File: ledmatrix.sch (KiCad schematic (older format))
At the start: 89 parts, among them U58 sled1735

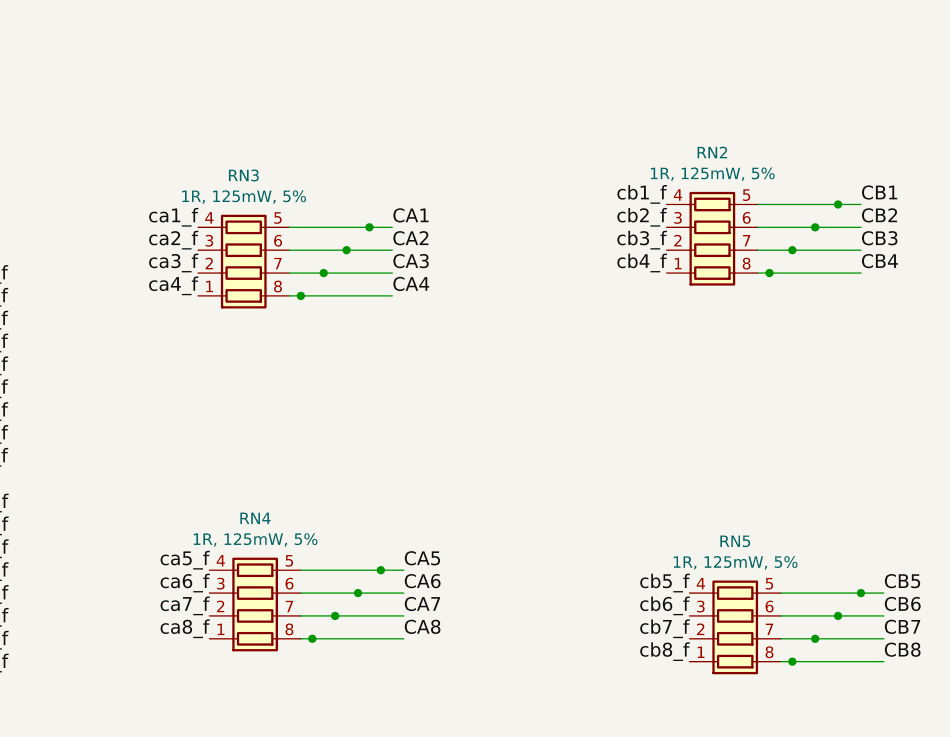
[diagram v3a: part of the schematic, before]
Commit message: changed 1nf filter caps to DNP, and resister packs to 0R, updated schematic date
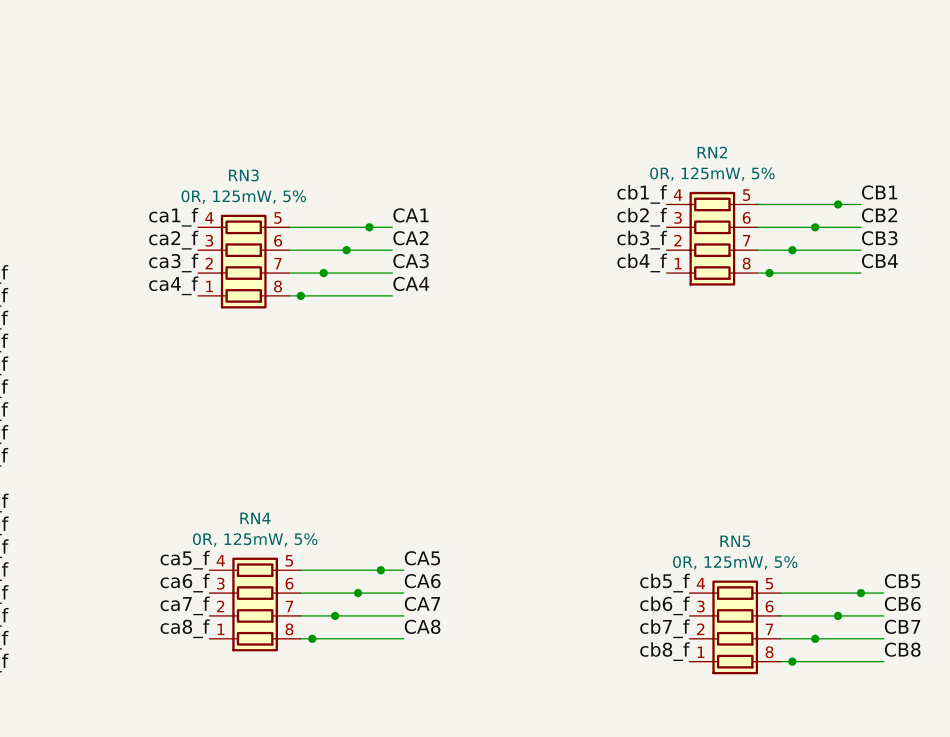
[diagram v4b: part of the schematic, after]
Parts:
- C16, C17, C19, C20, C21, C22, C23, C24, C25, C26, C27, C28, C29, C30, C31, C32, C35: supplier any/open -> dnp
- RN2, RN3, RN4, RN5: value 1R, 125mW, 5% -> 0R, 125mW, 5%
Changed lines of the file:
@@
 F 3 "" H 12550 8200 50  0000 C CNN
 F 4 "2896415" H 12550 8200 60  0001 C CNN "farnell #"
-F 5 "any/open" H 12550 8200 60  0001 C CNN "supplier"
+F 5 "dnp" H 12550 8200 60  0001 C CNN "supplier"
 F 6 "Value" H 12550 8200 60  0001 C CNN "supplier PN"
 F 7 "Value" H 12550 8200 60  0001 C CNN "MOQ"
@@
 P 12400 2000
 F 0 "RN3" V 12725 2000 50  0000 C CNN
-F 1 "1R, 125mW, 5%" V 12634 2000 50  0000 C CNN
+F 1 "0R, 125mW, 5%" V 12634 2000 50  0000 C CNN
 F 2 "raise_fp:R_Array_Convex_4x0402" V 12675 2000 50  0001 C CNN
 F 3 "" H 12400 2000 50  0001 C CNN
@@
 P 12450 3500
 F 0 "RN4" V 12775 3500 50  0000 C CNN
-F 1 "1R, 125mW, 5%" V 12684 3500 50  0000 C CNN
+F 1 "0R, 125mW, 5%" V 12684 3500 50  0000 C CNN
 F 2 "raise_fp:R_Array_Convex_4x0402" V 12725 3500 50  0001 C CNN
 F 3 "" H 12450 3500 50  0001 C CNN
@@
 P 14450 1900
 F 0 "RN2" V 14775 1900 50  0000 C CNN
-F 1 "1R, 125mW, 5%" V 14684 1900 50  0000 C CNN
+F 1 "0R, 125mW, 5%" V 14684 1900 50  0000 C CNN
 F 2 "raise_fp:R_Array_Convex_4x0402" V 14725 1900 50  0001 C CNN
 F 3 "" H 14450 1900 50  0001 C CNN
@@
 P 14550 3600
 F 0 "RN5" V 14875 3600 50  0000 C CNN
-F 1 "1R, 125mW, 5%" V 14784 3600 50  0000 C CNN
+F 1 "0R, 125mW, 5%" V 14784 3600 50  0000 C CNN
 F 2 "raise_fp:R_Array_Convex_4x0402" V 14825 3600 50  0001 C CNN
 F 3 "" H 14550 3600 50  0001 C CNN
@@
 F 3 "" H 12300 4700 50  0000 C CNN
 F 4 "2896415" H 12300 4700 60  0001 C CNN "farnell #"
-F 5 "any/open" H 12300 4700 60  0001 C CNN "supplier"
+F 5 "dnp" H 12300 4700 60  0001 C CNN "supplier"
 F 6 "Value" H 12300 4700 60  0001 C CNN "supplier PN"
 F 7 "Value" H 12300 4700 60  0001 C CNN "MOQ"
@@
 F 3 "" H 12500 4700 50  0000 C CNN
 F 4 "2896415" H 12500 4700 60  0001 C CNN "farnell #"
-F 5 "any/open" H 12500 4700 60  0001 C CNN "supplier"
+F 5 "dnp" H 12500 4700 60  0001 C CNN "supplier"
 F 6 "Value" H 12500 4700 60  0001 C CNN "supplier PN"
 F 7 "Value" H 12500 4700 60  0001 C CNN "MOQ"
@@
 F 3 "" H 12400 4950 50  0000 C CNN
 F 4 "2896415" H 12400 4950 60  0001 C CNN "farnell #"
-F 5 "any/open" H 12400 4950 60  0001 C CNN "supplier"
+F 5 "dnp" H 12400 4950 60  0001 C CNN "supplier"
 F 6 "Value" H 12400 4950 60  0001 C CNN "supplier PN"
 F 7 "Value" H 12400 4950 60  0001 C CNN "MOQ"
@@
 F 3 "" H 12600 4950 50  0000 C CNN
 F 4 "2896415" H 12600 4950 60  0001 C CNN "farnell #"
-F 5 "any/open" H 12600 4950 60  0001 C CNN "supplier"
+F 5 "dnp" H 12600 4950 60  0001 C CNN "supplier"
 F 6 "Value" H 12600 4950 60  0001 C CNN "supplier PN"
 F 7 "Value" H 12600 4950 60  0001 C CNN "MOQ"
@@
 F 3 "" H 12250 6100 50  0000 C CNN
 F 4 "2896415" H 12250 6100 60  0001 C CNN "farnell #"
-F 5 "any/open" H 12250 6100 60  0001 C CNN "supplier"
+F 5 "dnp" H 12250 6100 60  0001 C CNN "supplier"
 F 6 "Value" H 12250 6100 60  0001 C CNN "supplier PN"
 F 7 "Value" H 12250 6100 60  0001 C CNN "MOQ"
@@
 F 3 "" H 12450 6100 50  0000 C CNN
 F 4 "2896415" H 12450 6100 60  0001 C CNN "farnell #"
-F 5 "any/open" H 12450 6100 60  0001 C CNN "supplier"
+F 5 "dnp" H 12450 6100 60  0001 C CNN "supplier"
 F 6 "Value" H 12450 6100 60  0001 C CNN "supplier PN"
 F 7 "Value" H 12450 6100 60  0001 C CNN "MOQ"
@@
 F 3 "" H 12350 6350 50  0000 C CNN
 F 4 "2896415" H 12350 6350 60  0001 C CNN "farnell #"
-F 5 "any/open" H 12350 6350 60  0001 C CNN "supplier"
+F 5 "dnp" H 12350 6350 60  0001 C CNN "supplier"
 F 6 "Value" H 12350 6350 60  0001 C CNN "supplier PN"
 F 7 "Value" H 12350 6350 60  0001 C CNN "MOQ"
@@
 F 3 "" H 12550 6350 50  0000 C CNN
 F 4 "2896415" H 12550 6350 60  0001 C CNN "farnell #"
-F 5 "any/open" H 12550 6350 60  0001 C CNN "supplier"
+F 5 "dnp" H 12550 6350 60  0001 C CNN "supplier"
 F 6 "Value" H 12550 6350 60  0001 C CNN "supplier PN"
 F 7 "Value" H 12550 6350 60  0001 C CNN "MOQ"
@@
 F 3 "" H 14050 6050 50  0000 C CNN
 F 4 "2896415" H 14050 6050 60  0001 C CNN "farnell #"
-F 5 "any/open" H 14050 6050 60  0001 C CNN "supplier"
+F 5 "dnp" H 14050 6050 60  0001 C CNN "supplier"
 F 6 "Value" H 14050 6050 60  0001 C CNN "supplier PN"
 F 7 "Value" H 14050 6050 60  0001 C CNN "MOQ"
@@
 F 3 "" H 14250 6050 50  0000 C CNN
 F 4 "2896415" H 14250 6050 60  0001 C CNN "farnell #"
-F 5 "any/open" H 14250 6050 60  0001 C CNN "supplier"
+F 5 "dnp" H 14250 6050 60  0001 C CNN "supplier"
 F 6 "Value" H 14250 6050 60  0001 C CNN "supplier PN"
 F 7 "Value" H 14250 6050 60  0001 C CNN "MOQ"
@@
 F 3 "" H 14150 6300 50  0000 C CNN
 F 4 "2896415" H 14150 6300 60  0001 C CNN "farnell #"
-F 5 "any/open" H 14150 6300 60  0001 C CNN "supplier"
+F 5 "dnp" H 14150 6300 60  0001 C CNN "supplier"
 F 6 "Value" H 14150 6300 60  0001 C CNN "supplier PN"
 F 7 "Value" H 14150 6300 60  0001 C CNN "MOQ"
@@
 F 3 "" H 14350 6300 50  0000 C CNN
 F 4 "2896415" H 14350 6300 60  0001 C CNN "farnell #"
-F 5 "any/open" H 14350 6300 60  0001 C CNN "supplier"
+F 5 "dnp" H 14350 6300 60  0001 C CNN "supplier"
 F 6 "Value" H 14350 6300 60  0001 C CNN "supplier PN"
 F 7 "Value" H 14350 6300 60  0001 C CNN "MOQ"
@@
 F 3 "" H 14100 4650 50  0000 C CNN
 F 4 "2896415" H 14100 4650 60  0001 C CNN "farnell #"
-F 5 "any/open" H 14100 4650 60  0001 C CNN "supplier"
+F 5 "dnp" H 14100 4650 60  0001 C CNN "supplier"
 F 6 "Value" H 14100 4650 60  0001 C CNN "supplier PN"
 F 7 "Value" H 14100 4650 60  0001 C CNN "MOQ"
@@
 F 3 "" H 14300 4650 50  0000 C CNN
 F 4 "2896415" H 14300 4650 60  0001 C CNN "farnell #"
-F 5 "any/open" H 14300 4650 60  0001 C CNN "supplier"
+F 5 "dnp" H 14300 4650 60  0001 C CNN "supplier"
 F 6 "Value" H 14300 4650 60  0001 C CNN "supplier PN"
 F 7 "Value" H 14300 4650 60  0001 C CNN "MOQ"
@@
 F 3 "" H 14200 4900 50  0000 C CNN
 F 4 "2896415" H 14200 4900 60  0001 C CNN "farnell #"
-F 5 "any/open" H 14200 4900 60  0001 C CNN "supplier"
+F 5 "dnp" H 14200 4900 60  0001 C CNN "supplier"
 F 6 "Value" H 14200 4900 60  0001 C CNN "supplier PN"
 F 7 "Value" H 14200 4900 60  0001 C CNN "MOQ"
@@
 F 3 "" H 14400 4900 50  0000 C CNN
 F 4 "2896415" H 14400 4900 60  0001 C CNN "farnell #"
-F 5 "any/open" H 14400 4900 60  0001 C CNN "supplier"
+F 5 "dnp" H 14400 4900 60  0001 C CNN "supplier"
 F 6 "Value" H 14400 4900 60  0001 C CNN "supplier PN"
 F 7 "Value" H 14400 4900 60  0001 C CNN "MOQ"

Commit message: cleanup
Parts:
- R30: value 1R, 125mW, 5% -> 0R, 125mW, 5%
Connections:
- wire segments 104 -> 115
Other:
- note added: "optional output filters\n"
- moved on the sheet: C16, C17, C19, C20, C21, C22, C23, C24, C25, C26, C27, C28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

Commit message: bom consolidation
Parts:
- C10, C16, C17, C19, C20, C21, C22, C23, C24, C25, C26, C27, C28, C29, C30, C31, C32, C35, C6, R7: supplier PN Value -> (none)
- R30: supplier PN dnp -> (none)
- RN2, RN3, RN4, RN5: supplier Value -> any/open; supplier PN Value -> (none)
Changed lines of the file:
@@
 F 4 "2896426" H 9250 2100 60  0001 C CNN "farnell #"
 F 5 "any/open" H 550 0   60  0001 C CNN "supplier"
-F 6 "Value" H 9250 2100 60  0001 C CNN "supplier PN"
+F 6 "" H 9250 2100 60  0001 C CNN "supplier PN"
 F 7 "Value" H 9250 2100 60  0001 C CNN "MOQ"
 F 8 "Value" H 9250 2100 60  0001 C CNN "leadtime"
@@
 F 4 "2447230" H 9250 3450 60  0001 C CNN "farnell #"
 F 5 "any/open" H 9250 3450 60  0001 C CNN "supplier"
-F 6 "Value" H 9250 3450 60  0001 C CNN "supplier PN"
+F 6 "" H 9250 3450 60  0001 C CNN "supplier PN"
 F 7 "Value" H 9250 3450 60  0001 C CNN "MOQ"
 F 8 "Value" H 9250 3450 60  0001 C CNN "leadtime"
@@
 F 4 "dnp" H 12350 6550 60  0001 C CNN "farnell #"
 F 5 "dnp" H 12350 6550 60  0001 C CNN "supplier"
-F 6 "dnp" H 12350 6550 60  0001 C CNN "supplier PN"
+F 6 "" H 12350 6550 60  0001 C CNN "supplier PN"
 F 7 "Value" H 12350 6550 60  0001 C CNN "MOQ"
 F 8 "Value" H 12350 6550 60  0001 C CNN "leadtime"
@@
 F 4 "2896415" H 14750 4900 60  0001 C CNN "farnell #"
 F 5 "dnp" H 14750 4900 60  0001 C CNN "supplier"
-F 6 "Value" H 14750 4900 60  0001 C CNN "supplier PN"
+F 6 "" H 14750 4900 60  0001 C CNN "supplier PN"
 F 7 "Value" H 14750 4900 60  0001 C CNN "MOQ"
 F 8 "Value" H 14750 4900 60  0001 C CNN "leadtime"
@@
 F 2 "raise_fp:R_Array_Convex_4x0402" V 12675 2000 50  0001 C CNN
 F 3 "" H 12400 2000 50  0001 C CNN
-F 4 "Value" H 12400 2000 60  0001 C CNN "supplier"
-F 5 "Value" H 12400 2000 60  0001 C CNN "supplier PN"
+F 4 "any/open" H 12400 2000 60  0001 C CNN "supplier"
+F 5 "" H 12400 2000 60  0001 C CNN "supplier PN"
 F 6 "Value" H 12400 2000 60  0001 C CNN "MOQ"
 F 7 "Value" H 12400 2000 60  0001 C CNN "leadtime"
@@
 F 2 "raise_fp:R_Array_Convex_4x0402" V 12725 4150 50  0001 C CNN
 F 3 "" H 12450 4150 50  0001 C CNN
-F 4 "Value" H 12450 4150 60  0001 C CNN "supplier"
-F 5 "Value" H 12450 4150 60  0001 C CNN "supplier PN"
+F 4 "any/open" H 12450 4150 60  0001 C CNN "supplier"
+F 5 "" H 12450 4150 60  0001 C CNN "supplier PN"
 F 6 "Value" H 12450 4150 60  0001 C CNN "MOQ"
 F 7 "Value" H 12450 4150 60  0001 C CNN "leadtime"
@@
 F 2 "raise_fp:R_Array_Convex_4x0402" V 14725 2000 50  0001 C CNN
 F 3 "" H 14450 2000 50  0001 C CNN
-F 4 "Value" H 14450 2000 60  0001 C CNN "supplier"
-F 5 "Value" H 14450 2000 60  0001 C CNN "supplier PN"
+F 4 "any/open" H 14450 2000 60  0001 C CNN "supplier"
+F 5 "" H 14450 2000 60  0001 C CNN "supplier PN"
 F 6 "Value" H 14450 2000 60  0001 C CNN "MOQ"
 F 7 "Value" H 14450 2000 60  0001 C CNN "leadtime"
@@
 F 2 "raise_fp:R_Array_Convex_4x0402" V 14775 4150 50  0001 C CNN
 F 3 "" H 14500 4150 50  0001 C CNN
-F 4 "Value" H 14500 4150 60  0001 C CNN "supplier"
-F 5 "Value" H 14500 4150 60  0001 C CNN "supplier PN"
+F 4 "any/open" H 14500 4150 60  0001 C CNN "supplier"
+F 5 "" H 14500 4150 60  0001 C CNN "supplier PN"
 F 6 "Value" H 14500 4150 60  0001 C CNN "MOQ"
 F 7 "Value" H 14500 4150 60  0001 C CNN "leadtime"
@@
 F 4 "2896426" H 9600 2100 60  0001 C CNN "farnell #"
 F 5 "any/open" H 900 0   60  0001 C CNN "supplier"
-F 6 "Value" H 9600 2100 60  0001 C CNN "supplier PN"
+F 6 "" H 9600 2100 60  0001 C CNN "supplier PN"
 F 7 "Value" H 9600 2100 60  0001 C CNN "MOQ"
 F 8 "Value" H 9600 2100 60  0001 C CNN "leadtime"
@@
 F 4 "2896415" H 12950 2750 60  0001 C CNN "farnell #"
 F 5 "dnp" H 12950 2750 60  0001 C CNN "supplier"
-F 6 "Value" H 12950 2750 60  0001 C CNN "supplier PN"
+F 6 "" H 12950 2750 60  0001 C CNN "supplier PN"
 F 7 "Value" H 12950 2750 60  0001 C CNN "MOQ"
 F 8 "Value" H 12950 2750 60  0001 C CNN "leadtime"
@@
 F 4 "2896415" H 12750 2750 60  0001 C CNN "farnell #"
 F 5 "dnp" H 12750 2750 60  0001 C CNN "supplier"
-F 6 "Value" H 12750 2750 60  0001 C CNN "supplier PN"
+F 6 "" H 12750 2750 60  0001 C CNN "supplier PN"
 F 7 "Value" H 12750 2750 60  0001 C CNN "MOQ"
 F 8 "Value" H 12750 2750 60  0001 C CNN "leadtime"
@@
 F 4 "2896415" H 12850 3000 60  0001 C CNN "farnell #"
 F 5 "dnp" H 12850 3000 60  0001 C CNN "supplier"
-F 6 "Value" H 12850 3000 60  0001 C CNN "supplier PN"
+F 6 "" H 12850 3000 60  0001 C CNN "supplier PN"
 F 7 "Value" H 12850 3000 60  0001 C CNN "MOQ"
 F 8 "Value" H 12850 3000 60  0001 C CNN "leadtime"
@@
 F 4 "2896415" H 12650 3000 60  0001 C CNN "farnell #"
 F 5 "dnp" H 12650 3000 60  0001 C CNN "supplier"
-F 6 "Value" H 12650 3000 60  0001 C CNN "supplier PN"
+F 6 "" H 12650 3000 60  0001 C CNN "supplier PN"
 F 7 "Value" H 12650 3000 60  0001 C CNN "MOQ"
 F 8 "Value" H 12650 3000 60  0001 C CNN "leadtime"
@@
 F 4 "2896415" H 13000 4900 60  0001 C CNN "farnell #"
 F 5 "dnp" H 13000 4900 60  0001 C CNN "supplier"
-F 6 "Value" H 13000 4900 60  0001 C CNN "supplier PN"
+F 6 "" H 13000 4900 60  0001 C CNN "supplier PN"
 F 7 "Value" H 13000 4900 60  0001 C CNN "MOQ"
 F 8 "Value" H 13000 4900 60  0001 C CNN "leadtime"
@@
 F 4 "2896415" H 12800 4900 60  0001 C CNN "farnell #"
 F 5 "dnp" H 12800 4900 60  0001 C CNN "supplier"
-F 6 "Value" H 12800 4900 60  0001 C CNN "supplier PN"
+F 6 "" H 12800 4900 60  0001 C CNN "supplier PN"
 F 7 "Value" H 12800 4900 60  0001 C CNN "MOQ"
 F 8 "Value" H 12800 4900 60  0001 C CNN "leadtime"
@@
 F 4 "2896415" H 12900 5150 60  0001 C CNN "farnell #"
 F 5 "dnp" H 12900 5150 60  0001 C CNN "supplier"
-F 6 "Value" H 12900 5150 60  0001 C CNN "supplier PN"
+F 6 "" H 12900 5150 60  0001 C CNN "supplier PN"
 F 7 "Value" H 12900 5150 60  0001 C CNN "MOQ"
 F 8 "Value" H 12900 5150 60  0001 C CNN "leadtime"
@@
 F 4 "2896415" H 12700 5150 60  0001 C CNN "farnell #"
 F 5 "dnp" H 12700 5150 60  0001 C CNN "supplier"
-F 6 "Value" H 12700 5150 60  0001 C CNN "supplier PN"
+F 6 "" H 12700 5150 60  0001 C CNN "supplier PN"
 F 7 "Value" H 12700 5150 60  0001 C CNN "MOQ"
 F 8 "Value" H 12700 5150 60  0001 C CNN "leadtime"
@@
 F 4 "2896415" H 12900 6800 60  0001 C CNN "farnell #"
 F 5 "dnp" H 12900 6800 60  0001 C CNN "supplier"
-F 6 "Value" H 12900 6800 60  0001 C CNN "supplier PN"
+F 6 "" H 12900 6800 60  0001 C CNN "supplier PN"
 F 7 "Value" H 12900 6800 60  0001 C CNN "MOQ"
 F 8 "Value" H 12900 6800 60  0001 C CNN "leadtime"
@@
 F 4 "2896415" H 14900 2850 60  0001 C CNN "farnell #"
 F 5 "dnp" H 14900 2850 60  0001 C CNN "supplier"
-F 6 "Value" H 14900 2850 60  0001 C CNN "supplier PN"
+F 6 "" H 14900 2850 60  0001 C CNN "supplier PN"
 F 7 "Value" H 14900 2850 60  0001 C CNN "MOQ"
 F 8 "Value" H 14900 2850 60  0001 C CNN "leadtime"
@@
 F 4 "2896415" H 15000 3100 60  0001 C CNN "farnell #"
 F 5 "dnp" H 15000 3100 60  0001 C CNN "supplier"
-F 6 "Value" H 15000 3100 60  0001 C CNN "supplier PN"
+F 6 "" H 15000 3100 60  0001 C CNN "supplier PN"
 F 7 "Value" H 15000 3100 60  0001 C CNN "MOQ"
 F 8 "Value" H 15000 3100 60  0001 C CNN "leadtime"
@@
 F 4 "2896415" H 14800 3100 60  0001 C CNN "farnell #"
 F 5 "dnp" H 14800 3100 60  0001 C CNN "supplier"
-F 6 "Value" H 14800 3100 60  0001 C CNN "supplier PN"
+F 6 "" H 14800 3100 60  0001 C CNN "supplier PN"
 F 7 "Value" H 14800 3100 60  0001 C CNN "MOQ"
 F 8 "Value" H 14800 3100 60  0001 C CNN "leadtime"
@@
 F 4 "2896415" H 14700 2850 60  0001 C CNN "farnell #"
 F 5 "dnp" H 14700 2850 60  0001 C CNN "supplier"
-F 6 "Value" H 14700 2850 60  0001 C CNN "supplier PN"
+F 6 "" H 14700 2850 60  0001 C CNN "supplier PN"
 F 7 "Value" H 14700 2850 60  0001 C CNN "MOQ"
 F 8 "Value" H 14700 2850 60  0001 C CNN "leadtime"
@@
 F 4 "2896415" H 14950 4900 60  0001 C CNN "farnell #"
 F 5 "dnp" H 14950 4900 60  0001 C CNN "supplier"
-F 6 "Value" H 14950 4900 60  0001 C CNN "supplier PN"
+F 6 "" H 14950 4900 60  0001 C CNN "supplier PN"
 F 7 "Value" H 14950 4900 60  0001 C CNN "MOQ"
 F 8 "Value" H 14950 4900 60  0001 C CNN "leadtime"
@@
 F 4 "2896415" H 15050 5150 60  0001 C CNN "farnell #"
 F 5 "dnp" H 15050 5150 60  0001 C CNN "supplier"
-F 6 "Value" H 15050 5150 60  0001 C CNN "supplier PN"
+F 6 "" H 15050 5150 60  0001 C CNN "supplier PN"
 F 7 "Value" H 15050 5150 60  0001 C CNN "MOQ"
 F 8 "Value" H 15050 5150 60  0001 C CNN "leadtime"
@@
 F 4 "2896415" H 14850 5150 60  0001 C CNN "farnell #"
 F 5 "dnp" H 14850 5150 60  0001 C CNN "supplier"
-F 6 "Value" H 14850 5150 60  0001 C CNN "supplier PN"
+F 6 "" H 14850 5150 60  0001 C CNN "supplier PN"
 F 7 "Value" H 14850 5150 60  0001 C CNN "MOQ"
 F 8 "Value" H 14850 5150 60  0001 C CNN "leadtime"

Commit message: fixed wrong DNP 0R resistors
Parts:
- R30: farnell # dnp -> (none); supplier dnp -> any/open; supplier PN (none) -> Value
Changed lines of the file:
@@
 F 2 "raise_fp:R_0603" V 12280 6550 50  0001 C CNN
 F 3 "" H 12350 6550 50  0000 C CNN
-F 4 "dnp" H 12350 6550 60  0001 C CNN "farnell #"
-F 5 "dnp" H 12350 6550 60  0001 C CNN "supplier"
-F 6 "" H 12350 6550 60  0001 C CNN "supplier PN"
-F 7 "Value" H 12350 6550 60  0001 C CNN "MOQ"
-F 8 "Value" H 12350 6550 60  0001 C CNN "leadtime"
+F 4 "any/open" H 12350 6550 60  0001 C CNN "supplier"
+F 5 "Value" H 12350 6550 60  0001 C CNN "supplier PN"
+F 6 "Value" H 12350 6550 60  0001 C CNN "MOQ"
+F 7 "Value" H 12350 6550 60  0001 C CNN "leadtime"
 	1    12350 6550
 	0    1    1    0

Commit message: fix 0R names, set filter caps to virtual in PCB
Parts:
- R30: value 0R, 125mW, 5% -> 0R, 125mW, 5%
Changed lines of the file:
@@
 P 12350 6550
 F 0 "R30" V 12250 6500 50  0000 L CNN
-F 1 "0R,  125mW, 5%" V 12050 6300 50  0000 L CNN
+F 1 "0R, 125mW, 5%" V 12050 6300 50  0000 L CNN
 F 2 "raise_fp:R_0603" V 12280 6550 50  0001 C CNN
 F 3 "" H 12350 6550 50  0000 C CNN
